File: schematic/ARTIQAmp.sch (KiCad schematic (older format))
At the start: 0 parts

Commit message: Noodled around with KiCAD and added project-specific library
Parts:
- added R? (x3): R, symbol Device:R
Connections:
- net labels added: +48V, -45V, GND
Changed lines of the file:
@@
 EESchema Schematic File Version 4
+LIBS:ARTIQAmp-cache
 EELAYER 29 0
 EELAYER END
@@
 Comment4 ""
 $EndDescr
+$Comp
+L Device:R R?
+U 1 1 5C95ED26
+P 4350 3050
+F 0 "R?" H 4420 3096 50  0000 L CNN
+F 1 "R" H 4420 3005 50  0000 L CNN
+F 2 "" V 4280 3050 50  0001 C CNN
+F 3 "~" H 4350 3050 50  0001 C CNN
+	1    4350 3050
+	1    0    0    -1
+$EndComp
+$Comp
+L Device:R R?
+U 1 1 5C9603F1
+P 5050 2750
+F 0 "R?" H 5120 2796 50  0000 L CNN
+F 1 "R" H 5120 2705 50  0000 L CNN
+F 2 "" V 4980 2750 50  0001 C CNN
+F 3 "~" H 5050 2750 50  0001 C CNN
+	1    5050 2750
+	1    0    0    -1
+$EndComp
+$Comp
+L Device:R R?
+U 1 1 5C9606B7
+P 5900 3250
+F 0 "R?" H 5970 3296 50  0000 L CNN
+F 1 "R" H 5970 3205 50  0000 L CNN
+F 2 "" V 5830 3250 50  0001 C CNN
+F 3 "~" H 5900 3250 50  0001 C CNN
+	1    5900 3250
+	1    0    0    -1
+$EndComp
+$Comp
+L power:GND #PWR?
+U 1 1 5C9606FA
+P 4200 3800
+F 0 "#PWR?" H 4200 3550 50  0001 C CNN
+F 1 "GND" H 4205 3627 50  0000 C CNN
+F 2 "" H 4200 3800 50  0001 C CNN
+F 3 "" H 4200 3800 50  0001 C CNN
+	1    4200 3800
+	1    0    0    -1
+$EndComp
+$Comp
+L power:GND #PWR?
+U 1 1 5C960B25
+P 5850 3850
+F 0 "#PWR?" H 5850 3600 50  0001 C CNN
+F 1 "GND" H 5855 3677 50  0000 C CNN
+F 2 "" H 5850 3850 50  0001 C CNN
+F 3 "" H 5850 3850 50  0001 C CNN
+	1    5850 3850
+	1    0    0    -1
+$EndComp
+$Comp
+L power:+48V #PWR?
+U 1 1 5C960FC4
+P 3600 2250
+F 0 "#PWR?" H 3600 2100 50  0001 C CNN
+F 1 "+48V" H 3615 2423 50  0000 C CNN
+F 2 "" H 3600 2250 50  0001 C CNN
+F 3 "" H 3600 2250 50  0001 C CNN
+	1    3600 2250
+	1    0    0    -1
+$EndComp
+$Comp
+L test:-45V #PWR?
+U 1 1 5C961551
+P 3250 2800
+F 0 "#PWR?" H 3250 2900 50  0001 C CNN
+F 1 "-45V" H 3265 2973 50  0000 C CNN
+F 2 "" H 3250 2800 50  0001 C CNN
+F 3 "" H 3250 2800 50  0001 C CNN
+	1    3250 2800
+	1    0    0    -1
+$EndComp
 $EndSCHEMATC

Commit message: Added schematic, library and datasheets
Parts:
- removed R? (x3): R, symbol Device:R
- added J1, J2: Conn_Coaxial, symbol Connector:Conn_Coaxial
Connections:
- net labels added: VDD, VSS
- net labels removed: +48V, -45V
- wire segments 0 -> 7
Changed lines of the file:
@@
 $Descr A4 11693 8268
 encoding utf-8
-Sheet 1 1
+Sheet 1 2
 Title ""
 Date ""
@@
 $EndDescr
 $Comp
-L Device:R R?
-U 1 1 5C95ED26
-P 4350 3050
-F 0 "R?" H 4420 3096 50  0000 L CNN
-F 1 "R" H 4420 3005 50  0000 L CNN
-F 2 "" V 4280 3050 50  0001 C CNN
-F 3 "~" H 4350 3050 50  0001 C CNN
-	1    4350 3050
+L power:GND #PWR04
+U 1 1 5C960B25
+P 5350 1500
+F 0 "#PWR04" H 5350 1250 50  0001 C CNN
+F 1 "GND" H 5355 1327 50  0000 C CNN
+F 2 "" H 5350 1500 50  0001 C CNN
+F 3 "" H 5350 1500 50  0001 C CNN
+	1    5350 1500
+	1    0    0    -1
+$EndComp
+$Sheet
+S 6950 1800 700  300
+U 5C968447
+F0 "AmpBlock" 50
+F1 "AmpBlock.sch" 50
+F2 "INPUT" I L 6950 1900 50
+F3 "OUTPUT" I R 7650 2000 50
+$EndSheet
+$Comp
+L power:VSS #PWR0101
+U 1 1 5C983C61
+P 4950 1500
+F 0 "#PWR0101" H 4950 1350 50  0001 C CNN
+F 1 "VSS" H 4968 1673 50  0000 C CNN
+F 2 "" H 4950 1500 50  0001 C CNN
+F 3 "" H 4950 1500 50  0001 C CNN
+	1    4950 1500
+	-1   0    0    1
+$EndComp
+$Comp
+L power:PWR_FLAG #FLG0101
+U 1 1 5C984636
+P 4500 1400
+F 0 "#FLG0101" H 4500 1475 50  0001 C CNN
+F 1 "PWR_FLAG" H 4500 1573 50  0000 C CNN
+F 2 "" H 4500 1400 50  0001 C CNN
+F 3 "~" H 4500 1400 50  0001 C CNN
+	1    4500 1400
 	1    0    0    -1
 $EndComp
 $Comp
-L Device:R R?
-U 1 1 5C9603F1
-P 5050 2750
-F 0 "R?" H 5120 2796 50  0000 L CNN
-F 1 "R" H 5120 2705 50  0000 L CNN
-F 2 "" V 4980 2750 50  0001 C CNN
-F 3 "~" H 5050 2750 50  0001 C CNN
-	1    5050 2750
+L power:PWR_FLAG #FLG0102
+U 1 1 5C984DB2
+P 4950 1400
+F 0 "#FLG0102" H 4950 1475 50  0001 C CNN
+F 1 "PWR_FLAG" H 4950 1573 50  0000 C CNN
+F 2 "" H 4950 1400 50  0001 C CNN
+F 3 "~" H 4950 1400 50  0001 C CNN
+	1    4950 1400
 	1    0    0    -1
 $EndComp
 $Comp
-L Device:R R?
-U 1 1 5C9606B7
-P 5900 3250
-F 0 "R?" H 5970 3296 50  0000 L CNN
-F 1 "R" H 5970 3205 50  0000 L CNN
-F 2 "" V 5830 3250 50  0001 C CNN
-F 3 "~" H 5900 3250 50  0001 C CNN
-	1    5900 3250
+L power:PWR_FLAG #FLG0103
+U 1 1 5C985146
+P 5350 1400
+F 0 "#FLG0103" H 5350 1475 50  0001 C CNN
+F 1 "PWR_FLAG" H 5350 1573 50  0000 C CNN
+F 2 "" H 5350 1400 50  0001 C CNN
+F 3 "~" H 5350 1400 50  0001 C CNN
+	1    5350 1400
 	1    0    0    -1
 $EndComp
 $Comp
-L power:GND #PWR?
-U 1 1 5C9606FA
-P 4200 3800
-F 0 "#PWR?" H 4200 3550 50  0001 C CNN
-F 1 "GND" H 4205 3627 50  0000 C CNN
-F 2 "" H 4200 3800 50  0001 C CNN
-F 3 "" H 4200 3800 50  0001 C CNN
-	1    4200 3800
+L power:VDD #PWR0102
+U 1 1 5C985B3C
+P 4500 1500
+F 0 "#PWR0102" H 4500 1350 50  0001 C CNN
+F 1 "VDD" H 4518 1673 50  0000 C CNN
+F 2 "" H 4500 1500 50  0001 C CNN
+F 3 "" H 4500 1500 50  0001 C CNN
+	1    4500 1500
+	-1   0    0    1
+$EndComp
+Wire Wire Line
+	4500 1400 4500 1500
+Wire Wire Line
+	4950 1400 4950 1500
+Wire Wire Line
+	5350 1400 5350 1500
+$Comp
+L Connector:Conn_Coaxial J1
+U 1 1 5C986E23
+P 6400 1900
+F 0 "J1" H 6328 2138 50  0000 C CNN
+F 1 "Conn_Coaxial" H 6328 2047 50  0000 C CNN
+F 2 "" H 6400 1900 50  0001 C CNN
+F 3 " ~" H 6400 1900 50  0001 C CNN
+	1    6400 1900
+	-1   0    0    -1
+$EndComp
+$Comp
+L Connector:Conn_Coaxial J2
+U 1 1 5C9878F3
+P 8300 2000
+F 0 "J2" H 8400 1975 50  0000 L CNN
+F 1 "Conn_Coaxial" H 8400 1884 50  0000 L CNN
+F 2 "" H 8300 2000 50  0001 C CNN
+F 3 " ~" H 8300 2000 50  0001 C CNN
+	1    8300 2000
+	1    0    0    -1
+$EndComp
+Wire Wire Line
+	7650 2000 8100 2000
+Wire Wire Line
+	6600 1900 6950 1900
+$Comp
+L power:GND #PWR01
+U 1 1 5C988E83
+P 6400 2150
+F 0 "#PWR01" H 6400 1900 50  0001 C CNN
+F 1 "GND" H 6405 1977 50  0000 C CNN
+F 2 "" H 6400 2150 50  0001 C CNN
+F 3 "" H 6400 2150 50  0001 C CNN
+	1    6400 2150
 	1    0    0    -1
 $EndComp
 $Comp
-L power:GND #PWR?
-U 1 1 5C960B25
-P 5850 3850
-F 0 "#PWR?" H 5850 3600 50  0001 C CNN
-F 1 "GND" H 5855 3677 50  0000 C CNN
-F 2 "" H 5850 3850 50  0001 C CNN
-F 3 "" H 5850 3850 50  0001 C CNN
-	1    5850 3850
+L power:GND #PWR02
+U 1 1 5C9893C0
+P 8300 2250
+F 0 "#PWR02" H 8300 2000 50  0001 C CNN
+F 1 "GND" H 8305 2077 50  0000 C CNN
+F 2 "" H 8300 2250 50  0001 C CNN
+F 3 "" H 8300 2250 50  0001 C CNN
+	1    8300 2250
 	1    0    0    -1
 $EndComp
-$Comp
-L power:+48V #PWR?
-U 1 1 5C960FC4
-P 3600 2250
-F 0 "#PWR?" H 3600 2100 50  0001 C CNN
-F 1 "+48V" H 3615 2423 50  0000 C CNN
-F 2 "" H 3600 2250 50  0001 C CNN
-F 3 "" H 3600 2250 50  0001 C CNN
-	1    3600 2250
-	1    0    0    -1
-$EndComp
-$Comp
-L test:-45V #PWR?
-U 1 1 5C961551
-P 3250 2800
-F 0 "#PWR?" H 3250 2900 50  0001 C CNN
-F 1 "-45V" H 3265 2973 50  0000 C CNN
-F 2 "" H 3250 2800 50  0001 C CNN
-F 3 "" H 3250 2800 50  0001 C CNN
-	1    3250 2800
-	1    0    0    -1
-$EndComp
+Wire Wire Line
+	6400 2100 6400 2150
+Wire Wire Line
+	8300 2200 8300 2250
 $EndSCHEMATC

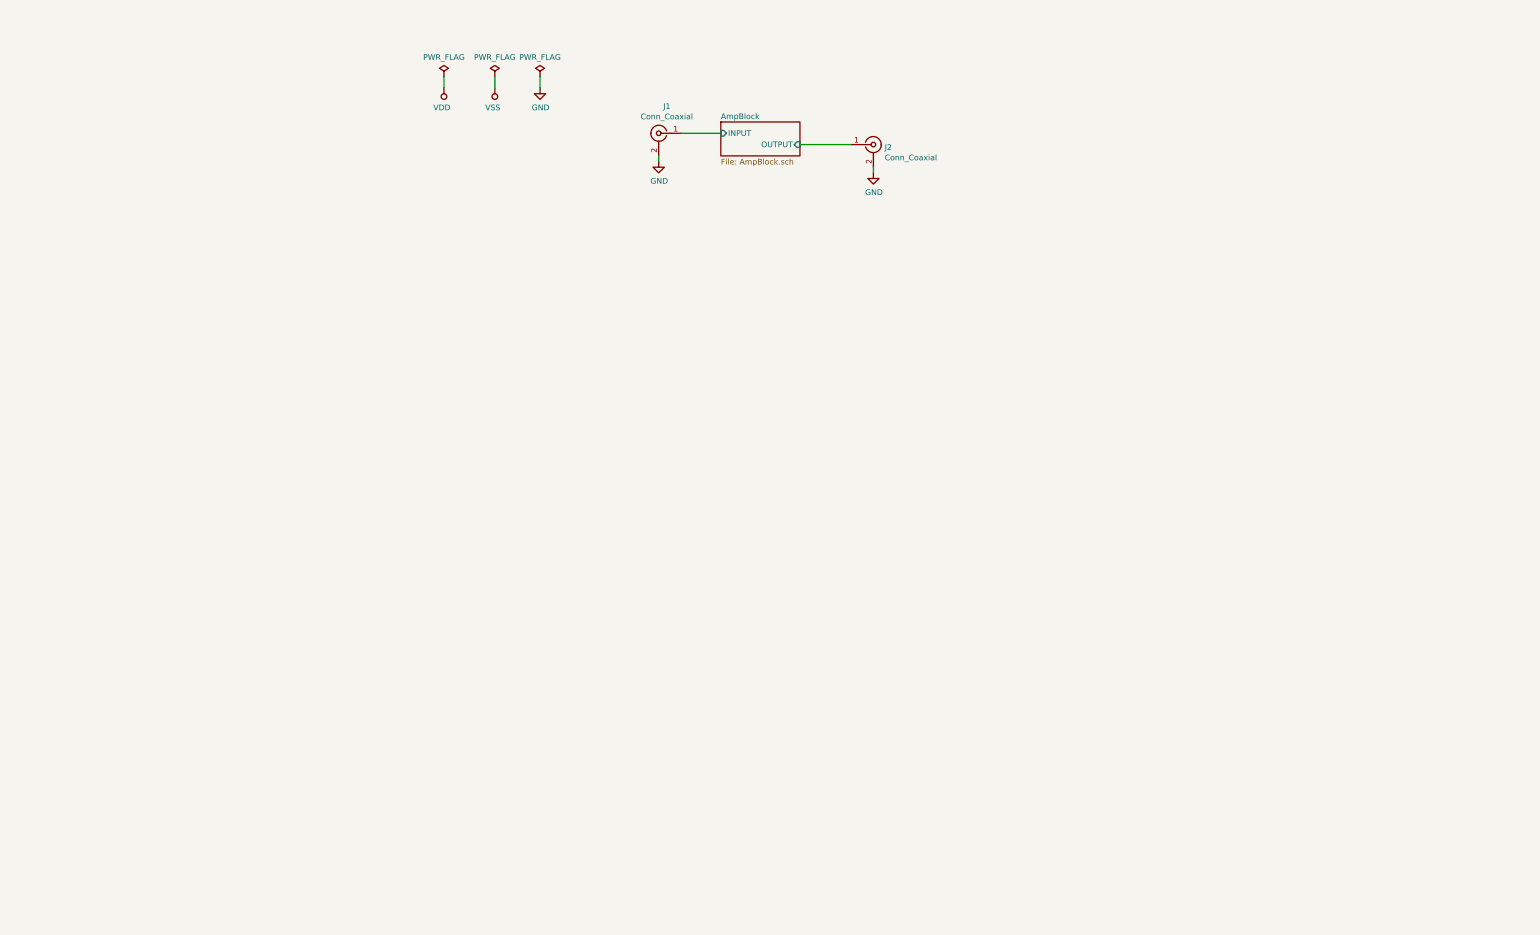
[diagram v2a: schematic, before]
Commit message: Added connectors to the library and made an array of lots of amps
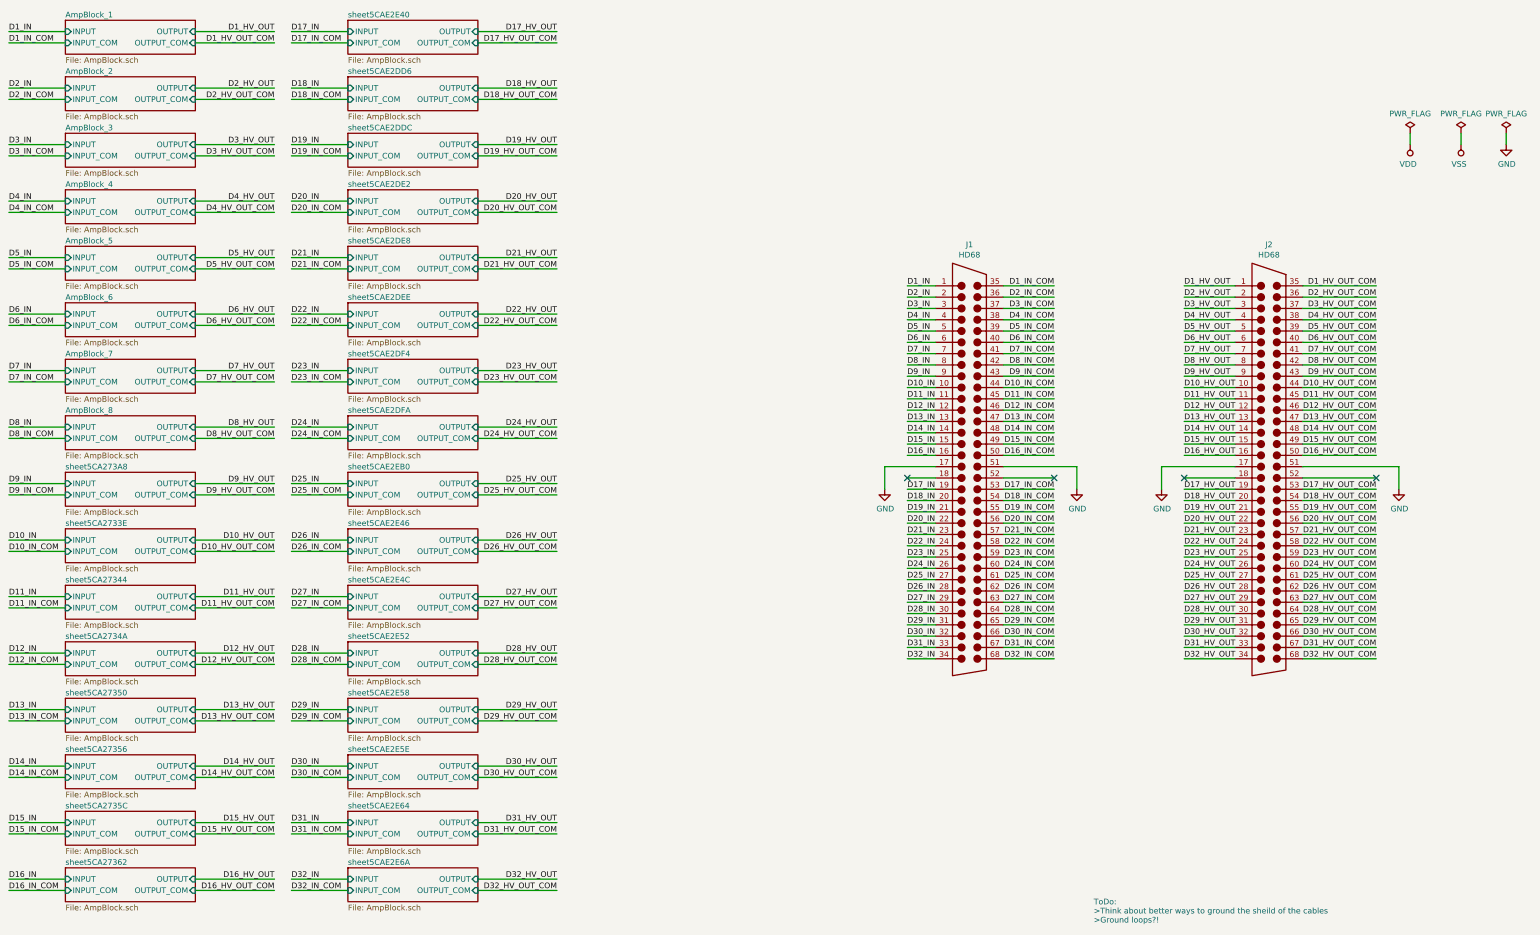
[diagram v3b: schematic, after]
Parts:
- removed J1, J2: Conn_Coaxial, symbol Connector:Conn_Coaxial
- added J1, J2: HD68, symbol ARTIQAmp:HD68
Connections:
- net GND: now also J1.17, J1.51, J2.17, J2.51
- new net D10_HV_OUT: J2.10
- new net D10_HV_OUT_COM: J2.44
- new net D10_IN: J1.10
- new net D10_IN_COM: J1.44
- new net D11_HV_OUT: J2.11
- new net D11_HV_OUT_COM: J2.45
- new net D11_IN: J1.11
- new net D11_IN_COM: J1.45
- new net D12_HV_OUT: J2.12
- new net D12_HV_OUT_COM: J2.46
- new net D12_IN: J1.12
- new net D12_IN_COM: J1.46
- new net D13_HV_OUT: J2.13
- new net D13_HV_OUT_COM: J2.47
- new net D13_IN: J1.13
- new net D13_IN_COM: J1.47
- new net D14_HV_OUT: J2.14
- new net D14_HV_OUT_COM: J2.48
- new net D14_IN: J1.14
- new net D14_IN_COM: J1.48
- new net D15_HV_OUT: J2.15
- new net D15_HV_OUT_COM: J2.49
- new net D15_IN: J1.15
- new net D15_IN_COM: J1.49
- new net D16_HV_OUT: J2.16
- new net D16_HV_OUT_COM: J2.50
- new net D16_IN: J1.16
- new net D16_IN_COM: J1.50
- new net D17_HV_OUT: J2.19
- new net D17_HV_OUT_COM: J2.53
- new net D17_IN: J1.19
- new net D17_IN_COM: J1.53
- new net D18_HV_OUT: J2.20
- new net D18_HV_OUT_COM: J2.54
- new net D18_IN: J1.20
- new net D18_IN_COM: J1.54
- new net D19_HV_OUT: J2.21
- new net D19_HV_OUT_COM: J2.55
- new net D19_IN: J1.21
- new net D19_IN_COM: J1.55
- new net D1_HV_OUT: J2.1
- new net D1_HV_OUT_COM: J2.35
- new net D1_IN: J1.1
- new net D1_IN_COM: J1.35
- new net D20_HV_OUT: J2.22
- new net D20_HV_OUT_COM: J2.56
- new net D20_IN: J1.22
- new net D20_IN_COM: J1.56
- new net D21_HV_OUT: J2.23
- new net D21_HV_OUT_COM: J2.57
- new net D21_IN: J1.23
- new net D21_IN_COM: J1.57
- new net D22_HV_OUT: J2.24
- new net D22_HV_OUT_COM: J2.58
- new net D22_IN: J1.24
- new net D22_IN_COM: J1.58
- new net D23_HV_OUT: J2.25
- new net D23_HV_OUT_COM: J2.59
- new net D23_IN: J1.25
- new net D23_IN_COM: J1.59
- new net D24_HV_OUT: J2.26
- new net D24_HV_OUT_COM: J2.60
- new net D24_IN: J1.26
- new net D24_IN_COM: J1.60
- new net D25_HV_OUT: J2.27
- new net D25_HV_OUT_COM: J2.61
- new net D25_IN: J1.27
- new net D25_IN_COM: J1.61
- new net D26_HV_OUT: J2.28
- new net D26_HV_OUT_COM: J2.62
- new net D26_IN: J1.28
- new net D26_IN_COM: J1.62
- new net D27_HV_OUT: J2.29
- new net D27_HV_OUT_COM: J2.63
- new net D27_IN: J1.29
- new net D27_IN_COM: J1.63
- new net D28_HV_OUT: J2.30
- new net D28_HV_OUT_COM: J2.64
- new net D28_IN: J1.30
- new net D28_IN_COM: J1.64
- new net D29_HV_OUT: J2.31
- new net D29_HV_OUT_COM: J2.65
- new net D29_IN: J1.31
- new net D29_IN_COM: J1.65
- new net D2_HV_OUT: J2.2
- new net D2_HV_OUT_COM: J2.36
- new net D2_IN: J1.2
- new net D2_IN_COM: J1.36
- new net D30_HV_OUT: J2.32
- new net D30_HV_OUT_COM: J2.66
- new net D30_IN: J1.32
- new net D30_IN_COM: J1.66
- new net D31_HV_OUT: J2.33
- new net D31_HV_OUT_COM: J2.67
- new net D31_IN: J1.33
- new net D31_IN_COM: J1.67
- new net D32_HV_OUT: J2.34
- new net D32_HV_OUT_COM: J2.68
- new net D32_IN: J1.34
- new net D32_IN_COM: J1.68
- new net D3_HV_OUT: J2.3
- new net D3_HV_OUT_COM: J2.37
- new net D3_IN: J1.3
- new net D3_IN_COM: J1.37
- new net D4_HV_OUT: J2.4
- new net D4_HV_OUT_COM: J2.38
- new net D4_IN: J1.4
- new net D4_IN_COM: J1.38
- new net D5_HV_OUT: J2.5
- new net D5_HV_OUT_COM: J2.39
- new net D5_IN: J1.5
- new net D5_IN_COM: J1.39
- new net D6_HV_OUT: J2.6
- new net D6_HV_OUT_COM: J2.40
- new net D6_IN: J1.6
- new net D6_IN_COM: J1.40
- new net D7_HV_OUT: J2.7
- new net D7_HV_OUT_COM: J2.41
- new net D7_IN: J1.7
- new net D7_IN_COM: J1.41
- new net D8_HV_OUT: J2.8
- new net D8_HV_OUT_COM: J2.42
- new net D8_IN: J1.8
- new net D8_IN_COM: J1.42
- new net D9_HV_OUT: J2.9
- new net D9_HV_OUT_COM: J2.43
- new net D9_IN: J1.9
- new net D9_IN_COM: J1.43
- no-connect marks 0 -> 4
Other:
- note added: "ToDo:\n>Think about better ways to ground the sheild of the cables\n>Ground loops?!"
